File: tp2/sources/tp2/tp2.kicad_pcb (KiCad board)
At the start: 2 copper layers, 60.5 x 40 mm, 26 parts, among them Q1 NPN, U1 LM324, U7 LM324

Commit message: tp2: agrega capacitores desacople y entrada alimentacion (xd)
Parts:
- added C3: 100n, Capacitor_THT:C_Disc_D6.0mm_W2.5mm_P5.00mm, F.Cu at (149.8, 76.0)
- added C4: 100n, Capacitor_THT:C_Disc_D6.0mm_W2.5mm_P5.00mm, F.Cu at (112.8, 78.0)
- added H7: MountingHole_Pad, TestPoint:TestPoint_THTPad_2.0x2.0mm_Drill1.0mm, F.Cu at (107.5, 80.7)
- moved H3 32.4 mm to (153.1, 80.7)
- moved R13 1.77 mm to (107.4, 48.1)
- moved H1 1.75 mm to (98.5, 49.5)
- moved R8 1.49 mm to (121.3, 48.3)
- moved C1 1.45 mm to (125.7, 48.2)
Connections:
- ? pad 1: (no net) -> Net-(U1D--)
- H2 pad 1: /V+ -> /Vin
- R12 pad 1: /V+ -> /Vin
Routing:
- net /V+: track 97.1 -> 87.7 mm
- net /Vin: track 0.00 -> 6.00 mm
- net 0: track 155.3 -> 158.5 mm
- net Net-(U1D--): track 28.3 -> 26.4 mm
- net Net-(U1A-+): track 54.2 -> 55.9 mm
- net Net-(R12-Pad2): track 13.1 -> 14.6 mm
- net Net-(C1-Pad1): track 10.8 -> 9.50 mm
- net Net-(U1C-+): track 16.2 -> 15.1 mm
- net /V_{in}: track 24.1 -> 25.1 mm
- net /Vout_{filter}: track 43.1 -> 42.3 mm

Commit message: tp2: agrega jumper entre Vcc y Vin
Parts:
- added JP1: Jumper_2_Open, Connector_PinHeader_2.54mm:PinHeader_1x02_P2.54mm_Vertical, F.Cu at (107.5, 72.3)
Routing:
- net /Vin: track 6.00 -> 18.0 mm
- net /V+: track 87.7 -> 93.8 mm

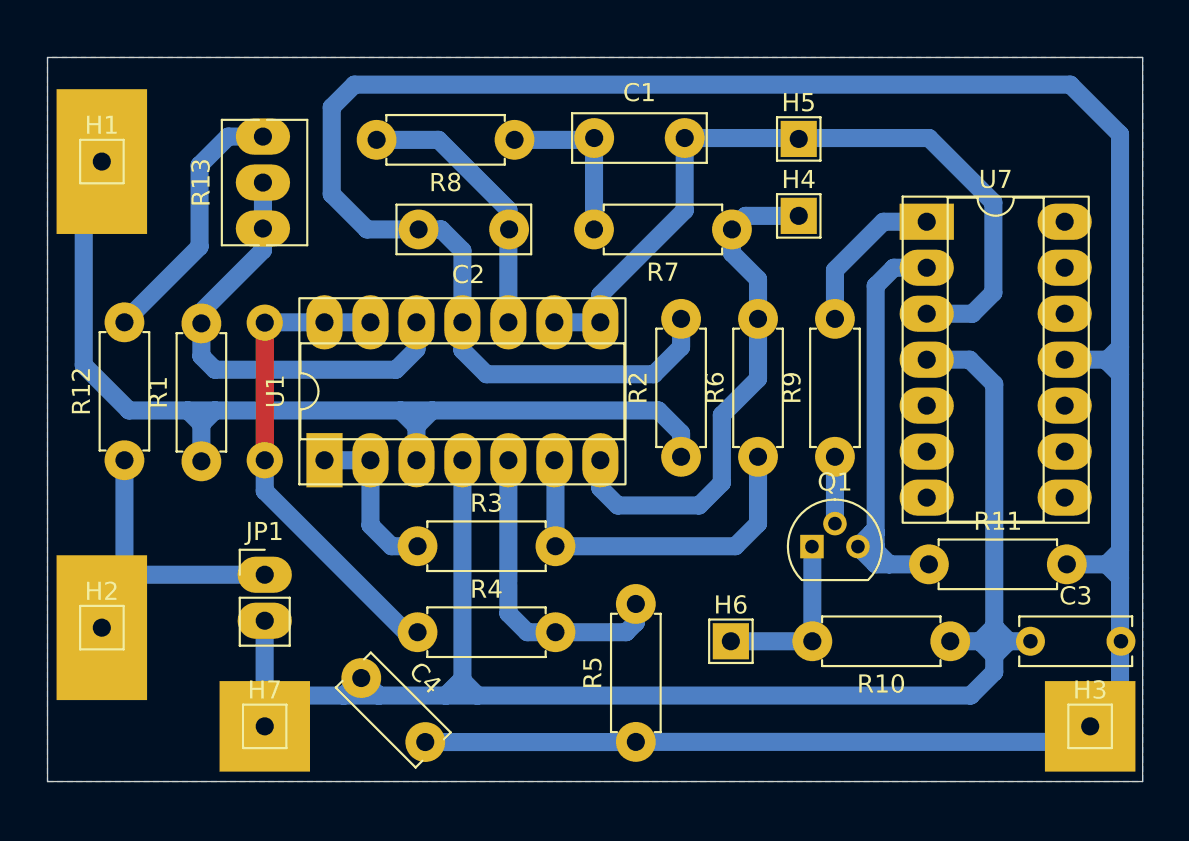
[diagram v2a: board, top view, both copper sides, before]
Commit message: tp2: reemplaza resistencias de 250ohm por (150+100)ohm
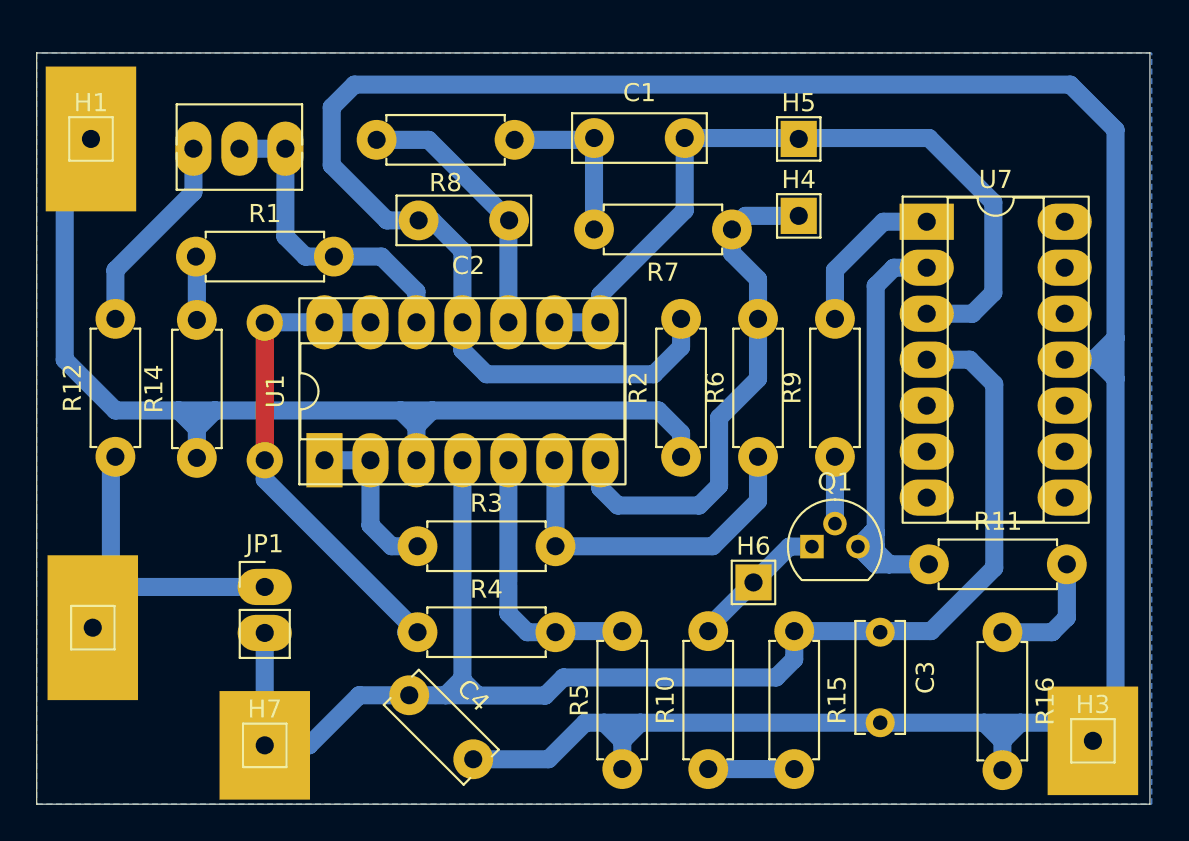
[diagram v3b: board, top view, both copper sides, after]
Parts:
- added R14: 100, Resistor_THT:R_Axial_DIN0207_L6.3mm_D2.5mm_P7.62mm_Horizontal, F.Cu at (103.8, 65.9)
- added R15: 100, Resistor_THT:R_Axial_DIN0207_L6.3mm_D2.5mm_P7.62mm_Horizontal, F.Cu at (136.8, 75.4)
- added R16: 150, Resistor_THT:R_Axial_DIN0207_L6.3mm_D2.5mm_P7.62mm_Horizontal, F.Cu at (148.2, 75.5)
- R1, R10: value 250 -> 150
- R11: value 250 -> 100
- moved R10 15.1 mm to (132.0, 83.1), turned to 90 degrees
- moved R1 11.3 mm to (103.7, 54.8), turned to 0 degrees
- moved C3 8.32 mm to (141.5, 75.5), turned to -90 degrees
- moved R13 3.90 mm to (103.6, 48.8), turned to 180 degrees
- moved H6 3.48 mm to (134.5, 72.8)
- moved C4 2.82 mm to (115.5, 79.0)
- moved R5 1.68 mm to (127.2, 83.1)
- moved H1 1.39 mm to (97.9, 48.2)
- moved H7 1.05 mm to (107.5, 81.8)
- moved H3 0.81 mm to (153.2, 81.5)
- moved JP1 0.67 mm to (107.5, 73.0)
- moved R12 0.53 mm to (99.2, 65.8)
- moved C2 0.50 mm to (116.0, 52.8)
- moved H2 0.50 mm to (98.0, 75.2)
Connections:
- R1 pad 1: Net-(U1A-+) -> Net-(R1-Pad1)
- R10 pad 1: /V+ -> Net-(R10-Pad1)
- R11 pad 2: 0 -> Net-(R11-Pad2)
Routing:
- net /V+: track 93.8 -> 80.0 mm
- net /V_{in}: track 25.1 -> 17.6 mm
- net Net-(R11-Pad2): track 0.00 -> 6.84 mm
- net Net-(R10-Pad1): track 0.00 -> 4.75 mm
- net Net-(R1-Pad1): track 0.00 -> 3.52 mm
- net Net-(R12-Pad2): track 14.6 -> 11.2 mm
- net Net-(U1A-+): track 55.9 -> 58.5 mm
- net 0: track 158.5 -> 161.0 mm
- net Net-(U1B-+): track 17.0 -> 15.0 mm
- net /V_{C}: track 9.74 -> 7.80 mm
- net Net-(U1B--): track 19.9 -> 19.2 mm
- net /Vin: track 18.0 -> 18.6 mm
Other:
- board size 60.5 x 40 mm -> 61.5 x 41.5 mm

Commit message: tp2: agrega jumper de gnd a la entrada Vin-
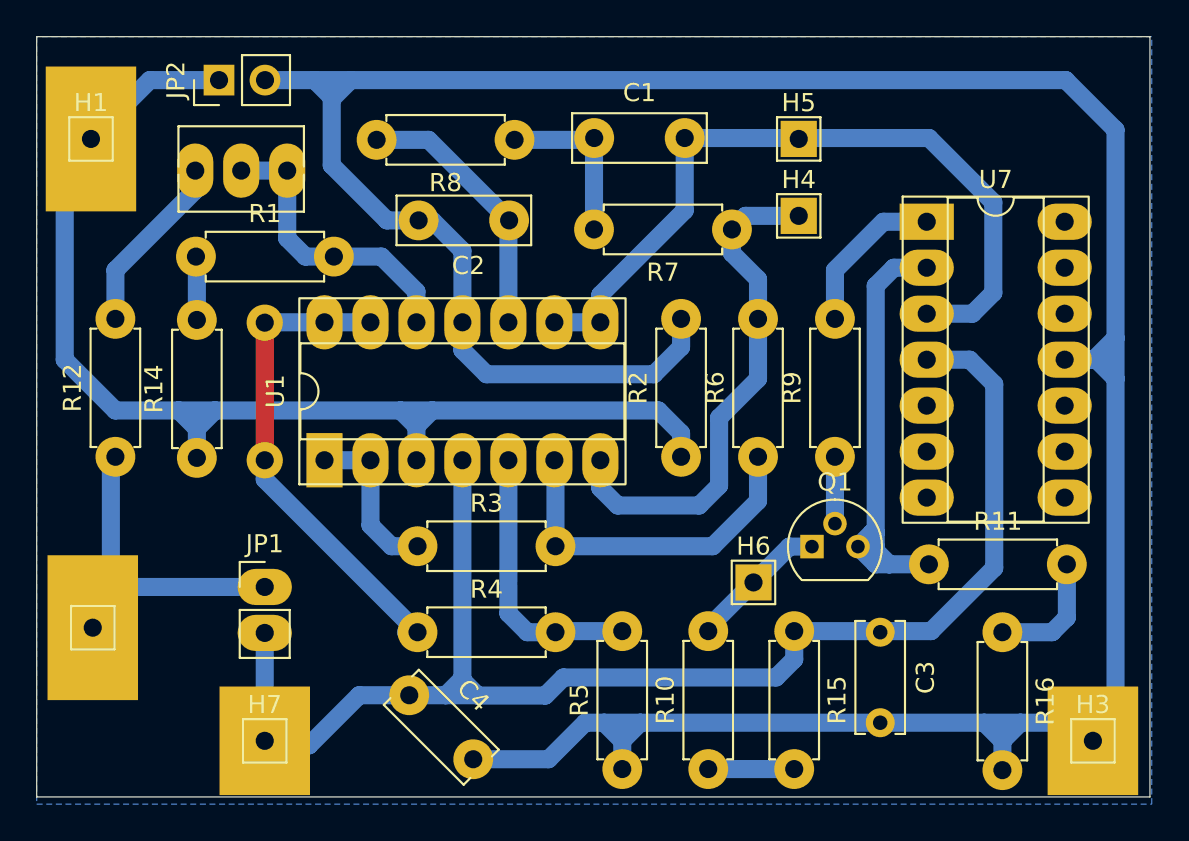
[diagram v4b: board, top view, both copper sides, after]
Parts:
- added JP2: Jumper_2_Open, Connector_PinHeader_2.54mm:PinHeader_1x02_P2.54mm_Vertical, F.Cu at (105.0, 45.0)
- moved R13 1.21 mm to (103.7, 50.0)
- moved H7 0.25 mm to (107.5, 81.5)
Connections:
- net Net-(U1A-+) renamed /Vin-
- H2 pad 1: /Vin -> /Vin+
- JP1 pad 1: /Vin -> /Vin+
- R1 pad 2: /V_{in} -> /Vin
- R12 pad 1: /Vin -> /Vin+
- R13 pad 2: /V_{in} -> /Vin
- R13 pad 3: /V_{in} -> /Vin
- U1 pad 12: /V_{in} -> /Vin
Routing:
- net /Vin+: track 0.00 -> 18.6 mm
- net /V_{in}: track 17.6 -> 0.00 mm
- net /Vin-: track 58.5 -> 66.9 mm
- net 0: track 161.0 -> 167.6 mm
- net /Vin: track 18.6 -> 16.3 mm
- net Net-(R12-Pad2): track 11.2 -> 10.0 mm
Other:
- board size 61.5 x 41.5 mm -> 61.5 x 42 mm

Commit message: tp2: achica 0.5mm (cero punto cinco milimietros) la placa
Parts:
- moved H7 0.32 mm to (107.6, 81.2)
- moved H3 0.30 mm to (153.3, 81.2)
- moved H1 0.20 mm to (98.1, 48.2)
- moved H2 0.11 mm to (98.1, 75.2)
- moved R16 0.10 mm to (148.2, 75.4)
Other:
- board size 61.5 x 42 mm -> 61.5 x 41.5 mm
